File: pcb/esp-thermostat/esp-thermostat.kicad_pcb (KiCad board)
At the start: 2 copper layers, 87 x 87 mm, 55 parts, among them J1 AC IN, J2 RELAY, J3 OLED, J4 PROGRAM, K1 HK4100F-DC5V-SHG, Q1 SS8050-G, Q2 SS8050-G, Q3 AO3480, SW1 SW_PLUS, SW2 SW_BOOST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

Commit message: Small improvements on the PCB
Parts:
- turned BT1 to 0 degrees
- turned R3 to 90 degrees
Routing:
- net ESP_RELAY: track 41.8 -> 44.8 mm
- net +3V3: track 225.2 -> 227.7 mm
- net ESP_SCL: track 103.5 -> 105.7 mm
- net ESP_SDA: track 98.4 -> 100.1 mm
- net Net-(Q3-Pad1): track 4.28 -> 2.98 mm
- net Net-(C1-Pad2): track 37.3 -> 36.0 mm
- net ESP_GPIO0: track 61.8 -> 62.6 mm
- net GND: vias 17 -> 28
- net (no net): vias 0 -> 1
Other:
- outline, holes or cut-outs redrawn

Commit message: Small improvements on the PCB
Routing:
- net Net-(D1-Pad1): track 22.4 -> 21.6 mm
- net GND: vias 28 -> 33
- net (no net): vias 1 -> 0
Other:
- outline, holes or cut-outs redrawn
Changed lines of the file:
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@@
   (general
     (thickness 1.6)
-    (drawings 32)
-    (tracks 531)
+    (drawings 36)
+    (tracks 541)
     (zones 0)
     (modules 55)
@@
   )
   (setup
-    (last_trace_width 0.3048)
+    (last_trace_width 0.8128)
     (user_trace_width 0.3048)
     (user_trace_width 0.4064)
@@
       (psa4output false)
       (plotreference true)
-      (plotvalue true)
+      (plotvalue false)
       (plotinvisibletext false)
       (padsonsilk false)
@@
       (outputformat 1)
       (mirror false)
-      (drillshape 1)
+      (drillshape 0)
       (scaleselection 1)
       (outputdirectory ""))
@@
     )
   )
+  (gr_line (start 25.4 40.2) (end 25.4 39.8) (layer Edge.Cuts) (width 0.05))
+  (gr_line (start 23.2 40.2) (end 25.4 40.2) (layer Edge.Cuts) (width 0.05))
+  (gr_line (start 23.2 39.8) (end 23.2 40.2) (layer Edge.Cuts) (width 0.05))
+  (gr_line (start 25.4 39.8) (end 23.2 39.8) (layer Edge.Cuts) (width 0.05))
   (gr_line (start 86 53) (end 86 55) (layer Edge.Cuts) (width 0.05))
   (gr_line (start 85 53) (end 85 55) (layer Edge.Cuts) (width 0.05))
@@
     (effects (font (size 1.5 1.5) (thickness 0.2)))
   )
-  (via (at 71.5 59.7) (size 0.8) (drill 0.4) (layers F.Cu B.Cu) (net 0))
   (segment (start 54.4 89.475) (end 54.45 89.425) (width 0.4064) (layer F.Cu) (net 7))
   (segment (start 54.4 91.7) (end 54.4 89.475) (width 0.4064) (layer F.Cu) (net 7))
@@
   (segment (start 26.7 45.3) (end 26.7 44.35) (width 0.8128) (layer F.Cu) (net 9))
   (segment (start 26.7 45.3) (end 26.7 46.25) (width 0.8128) (layer F.Cu) (net 9))
-  (segment (start 32.02 31.08) (end 34.46 31.08) (width 0.8128) (layer F.Cu) (net 9))
-  (segment (start 29.55 45.3) (end 29.55 33.55) (width 0.8128) (layer F.Cu) (net 9))
-  (segment (start 29.55 33.55) (end 32.02 31.08) (width 0.8128) (layer F.Cu) (net 9))
+  (segment (start 33.39934 31.08) (end 31.6 32.87934) (width 0.8128) (layer F.Cu) (net 9))
+  (segment (start 34.46 31.08) (end 33.39934 31.08) (width 0.8128) (layer F.Cu) (net 9))
+  (segment (start 31.6 32.87934) (end 31.6 40.8) (width 0.8128) (layer F.Cu) (net 9))
+  (segment (start 29.55 42.85) (end 29.55 45.3) (width 0.8128) (layer F.Cu) (net 9))
+  (segment (start 31.6 40.8) (end 29.55 42.85) (width 0.8128) (layer F.Cu) (net 9))
   (segment (start 34.925 46.25) (end 35 46.325) (width 0.3048) (layer F.Cu) (net 10))
   (segment (start 32.05 46.25) (end 34.925 46.25) (width 0.3048) (layer F.Cu) (net 10))
@@
   (via (at 35.5 66.9) (size 0.5) (drill 0.3) (layers F.Cu B.Cu) (net 21))
   (via (at 29.3 72.2) (size 0.5) (drill 0.3) (layers F.Cu B.Cu) (net 21))
-  (via (at 28.3 77.6) (size 0.5) (drill 0.3) (layers F.Cu B.Cu) (net 21))
-  (via (at 43.9 59) (size 0.5) (drill 0.3) (layers F.Cu B.Cu) (net 21))
-  (via (at 33.4 55.6) (size 0.5) (drill 0.3) (layers F.Cu B.Cu) (net 21))
-  (via (at 37.9 100.9) (size 0.5) (drill 0.3) (layers F.Cu B.Cu) (net 21))
-  (via (at 35.2 94.2) (size 0.5) (drill 0.3) (layers F.Cu B.Cu) (net 21))
+  (via (at 38.5 101) (size 0.5) (drill 0.3) (layers F.Cu B.Cu) (net 21))
+  (via (at 35.2 94) (size 0.5) (drill 0.3) (layers F.Cu B.Cu) (net 21))
   (via (at 39.2 94) (size 0.5) (drill 0.3) (layers F.Cu B.Cu) (net 21))
   (via (at 50.1 85.3) (size 0.5) (drill 0.3) (layers F.Cu B.Cu) (net 21))
   (via (at 45.8 85.4) (size 0.5) (drill 0.3) (layers F.Cu B.Cu) (net 21))
   (via (at 56.4 85.5) (size 0.5) (drill 0.3) (layers F.Cu B.Cu) (net 21))
-  (via (at 44.2 88.1) (size 0.5) (drill 0.3) (layers F.Cu B.Cu) (net 21))
+  (via (at 40.1 88.1) (size 0.5) (drill 0.3) (layers F.Cu B.Cu) (net 21))
   (via (at 31.7 63.9) (size 0.5) (drill 0.3) (layers F.Cu B.Cu) (net 21))
   (via (at 57.7 26.8) (size 0.8) (drill 0.4) (layers F.Cu B.Cu) (net 21))
@@
   (via (at 28.7 99.2) (size 0.8) (drill 0.4) (layers F.Cu B.Cu) (net 21))
   (via (at 74.9 96.6) (size 0.8) (drill 0.4) (layers F.Cu B.Cu) (net 21))
+  (via (at 46.3 60) (size 0.8) (drill 0.4) (layers F.Cu B.Cu) (net 21))
+  (via (at 42 64.8) (size 0.8) (drill 0.4) (layers F.Cu B.Cu) (net 21))
+  (via (at 26.9 77.3) (size 0.8) (drill 0.4) (layers F.Cu B.Cu) (net 21))
+  (via (at 50.2 88.3) (size 0.5) (drill 0.3) (layers F.Cu B.Cu) (net 21))
+  (via (at 50.3 94.6) (size 0.5) (drill 0.3) (layers F.Cu B.Cu) (net 21))
+  (via (at 57.2 80.4) (size 0.5) (drill 0.3) (layers F.Cu B.Cu) (net 21))
+  (via (at 40.2 98) (size 0.5) (drill 0.3) (layers F.Cu B.Cu) (net 21))
+  (via (at 44.3 98.2) (size 0.5) (drill 0.3) (layers F.Cu B.Cu) (net 21))
   (segment (start 36.154998 71.1) (end 35.554999 70.500001) (width 0.4064) (layer F.Cu) (net 22))
   (segment (start 37.55 71.1) (end 36.154998 71.1) (width 0.4064) (layer F.Cu) (net 22))
@@
   (segment (start 35.702401 99.997599) (end 35.7 100) (width 0.3048) (layer B.Cu) (net 27))
   (segment (start 46.3 100) (end 46.297599 99.997599) (width 0.3048) (layer B.Cu) (net 27))
-  (segment (start 46.297599 99.997599) (end 35.702401 99.997599) (width 0.3048) (layer B.Cu) (net 27))
   (segment (start 34.679 100) (end 34.254 99.575) (width 0.3048) (layer F.Cu) (net 27))
   (segment (start 35.7 100) (end 34.679 100) (width 0.3048) (layer F.Cu) (net 27))
+  (segment (start 46.1 100.2) (end 46.3 100) (width 0.3048) (layer B.Cu) (net 27))
+  (segment (start 36.1 100.2) (end 46.1 100.2) (width 0.3048) (layer B.Cu) (net 27))
+  (segment (start 35.7 100) (end 35.9 100) (width 0.3048) (layer B.Cu) (net 27))
+  (segment (start 35.9 100) (end 36.1 100.2) (width 0.3048) (layer B.Cu) (net 27))
   (segment (start 36.2 93.6) (end 36.2 95.3) (width 0.3048) (layer F.Cu) (net 28))
   (segment (start 36.2 92.225) (end 36.2 93.6) (width 0.3048) (layer B.Cu) (net 28))
@@
   (segment (start 42.2 98.2) (end 42.2 95.3) (width 0.3048) (layer F.Cu) (net 35))
   (segment (start 32.61443 99.327294) (end 32.61443 101.900522) (width 0.3048) (layer B.Cu) (net 35))
-  (segment (start 39.1 98.2) (end 38.597599 98.702401) (width 0.3048) (layer B.Cu) (net 35))
-  (segment (start 42.2 98.2) (end 39.1 98.2) (width 0.3048) (layer B.Cu) (net 35))
-  (segment (start 38.597599 98.702401) (end 37.702401 98.702401) (width 0.3048) (layer B.Cu) (net 35))
-  (segment (start 37.702401 98.702401) (end 37.20962 98.20962) (width 0.3048) (layer B.Cu) (net 35))
   (segment (start 37.20962 98.20962) (end 33.732104 98.20962) (width 0.3048) (layer B.Cu) (net 35))
   (segment (start 33.732104 98.20962) (end 32.61443 99.327294) (width 0.3048) (layer B.Cu) (net 35))
@@
   (segment (start 91 87.2) (end 96.4 87.2) (width 0.3048) (layer F.Cu) (net 35))
   (segment (start 74.95 78.9654) (end 84.05 78.9654) (width 0.3048) (layer B.Cu) (net 35))
+  (segment (start 42.2 98.2) (end 41.7 98.7) (width 0.3048) (layer B.Cu) (net 35))
+  (segment (start 41.7 98.7) (end 39 98.7) (width 0.3048) (layer B.Cu) (net 35))
+  (segment (start 39 98.7) (end 38.8 98.9) (width 0.3048) (layer B.Cu) (net 35))
+  (segment (start 37.9 98.9) (end 37.20962 98.20962) (width 0.3048) (layer B.Cu) (net 35))
+  (segment (start 38.8 98.9) (end 37.9 98.9) (width 0.3048) (layer B.Cu) (net 35))
   (via (at 44.2 93.6) (size 0.5) (drill 0.3) (layers F.Cu B.Cu) (net 36))
   (segment (start 44.2 92.225) (end 44.2 93.6) (width 0.3048) (layer B.Cu) (net 36))

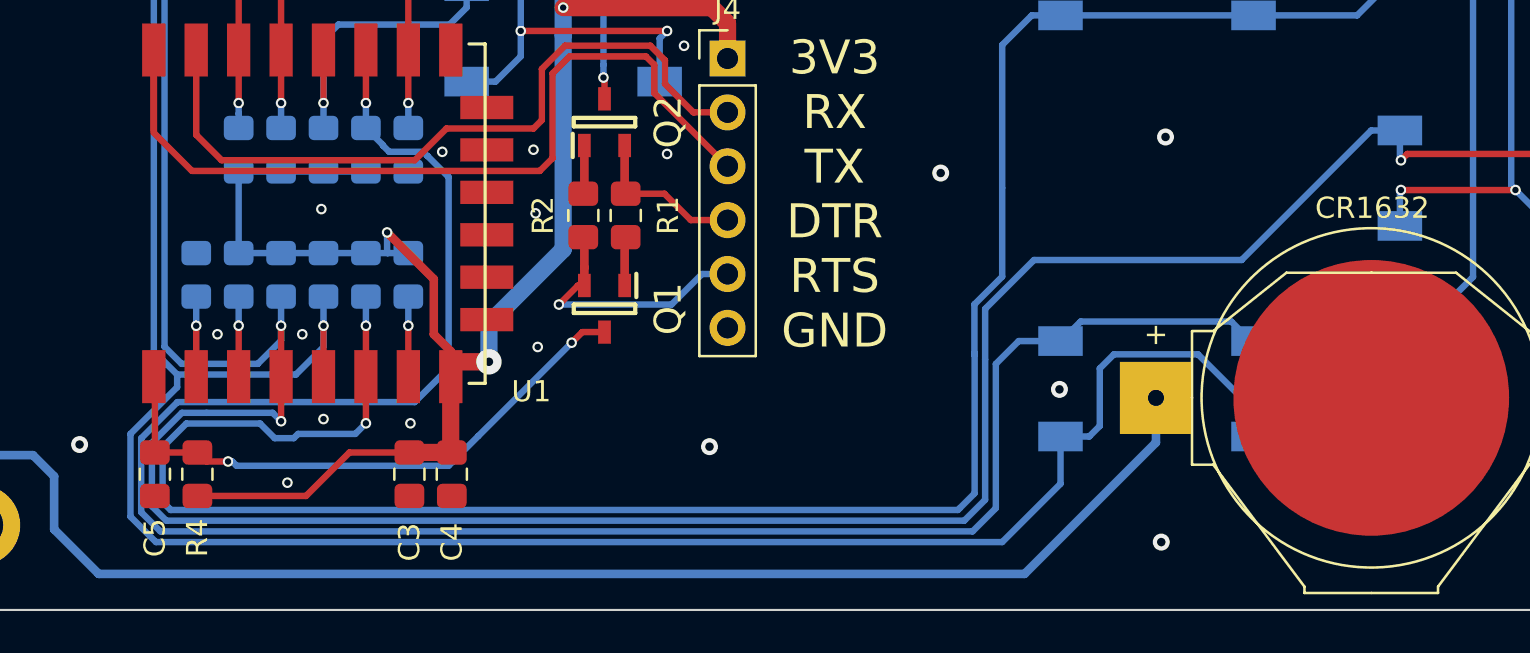
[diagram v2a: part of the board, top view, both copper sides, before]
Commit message: PCB: add temp sensor header, optimize routing
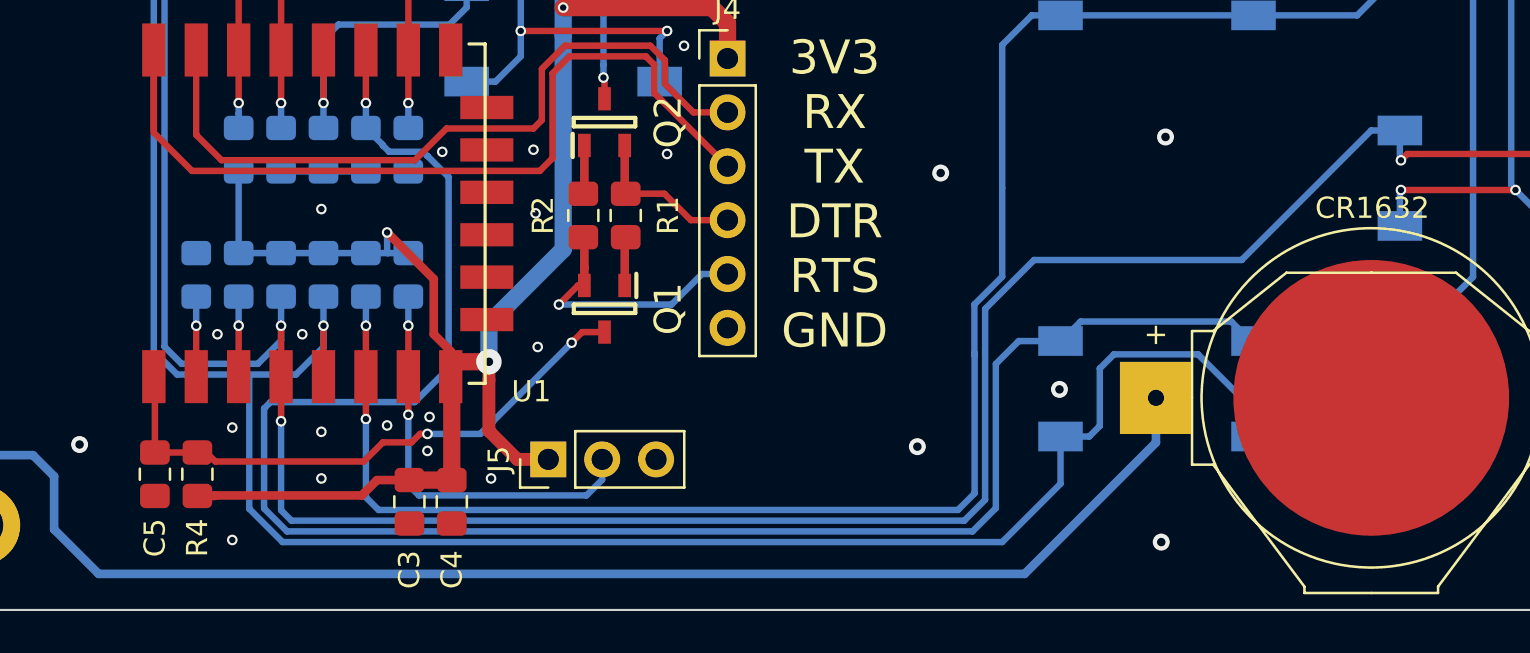
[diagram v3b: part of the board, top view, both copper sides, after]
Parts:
- added J5: DS18B20+, Connector_PinHeader_2.54mm:PinHeader_1x03_P2.54mm_Vertical, F.Cu at (50.8, 99.9)
- moved C3 1.30 mm to (44.2, 101.9)
- moved C4 1.30 mm to (46.2, 101.9)
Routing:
- net ESP_GPIO12: track 151.6 -> 131.8 mm
- net ESP_1W_DQ: track 3.08 -> 19.5 mm, vias 1 -> 2
- net ESP_GPIO16: track 146.9 -> 135.1 mm
- net ESP_GPIO2: track 145.0 -> 134.1 mm
- net +3V3: track 227.7 -> 235.1 mm
- net ESP_GPIO14: track 155.7 -> 149.0 mm
- net GND: vias 33 -> 38

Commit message: PCB: prepare for manufacturing
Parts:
- added C10: 100n, Capacitor_SMD:C_0805_2012Metric_Pad1.15x1.40mm_HandSolder, F.Cu at (71.4, 24.0)
- added C11: 100n, Capacitor_SMD:C_0805_2012Metric_Pad1.15x1.40mm_HandSolder, F.Cu at (59.5, 99.5)
- added C9: 1000u, Capacitor_THT:CP_Radial_D10.0mm_P5.00mm, F.Cu at (44.5, 56.4)
- BT1: value Battery_Cell -> 3V CR1632
- H1, H2, H3, H4, H5: footprint MountingHole:MountingHole_2.2mm_M2_ISO14580_Pad -> MountingHole:MountingHole_3.2mm_M3_ISO14580_Pad
- U3: value 47L04 -> 47L16
- moved J5 12.1 mm to (62.9, 99.5)
- moved C2 4.67 mm to (44.5, 50.1)
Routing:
- net Net-(BT1-Pad1): track 101.0 -> 126.8 mm
- net +3V3: track 235.1 -> 251.9 mm
- net GND: track 23.6 -> 39.1 mm, vias 38 -> 34
- net ESP_1W_DQ: track 19.5 -> 32.2 mm
- net Net-(J2-Pad3): track 11.5 -> 13.0 mm
- net ESP_GPIO14: track 149.0 -> 148.3 mm
- net ESP_GPIO0: track 62.6 -> 63.1 mm
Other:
- outline, holes or cut-outs redrawn
- net class Default: clearance 0.2 -> 0.1; trace_width 0.25 -> 0.3048; via_dia 0.8 -> 0.5; via_drill 0.4 -> 0.3
- net class GND added: clearance 0.05, trace_width 0.09, via_dia 0.5, via_drill 0.3
- net class High voltage: clearance 5 -> 0.1; trace_width 4 -> 1.27
- net class Signal: clearance 0.2 -> 0.1; via_dia 0.8 -> 0.5; via_drill 0.4 -> 0.3
- net class Supply voltage: clearance 0.2 -> 0.1
- rule trace_clearance: 0.2 -> 0.1
- rule trace_min: 0.2 -> 0.09
- rule via_min_drill: 0.3 -> 0.2
- rule via_min_size: 0.4 -> 0.45
- board text added: "0.5A 250V"
- board text added: "3V3 DQ GND"
- board text added: "47L16"
- board text added: "DS1307"
- board text added: "DS18B20+"
- board text added: "ESP-Thermostat v1.0 2020 - github.com/tomikaa87"
- board text added: "ESP12F"
- board text added: "JLCJLCJLCJLC"
- board text added: "OLED"
- board text added: "PROGRAM"
- board text removed: "ESP-Thermostat v1.0 2019 - github.com/tomikaa87"
